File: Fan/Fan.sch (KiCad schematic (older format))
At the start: 6 parts

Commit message: Added Fan Testing Circuit
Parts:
- added Q?: ZVN3306F, Package_TO_SOT_SMD:SOT-23, symbol Transistor_FET:ZVN3306F
- added R?: R, symbol Device:R
- added V?: SQUARE_WAVE, symbol pspice:VSOURCE
- added V?: 12V, symbol pspice:VSOURCE
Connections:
- net labels added: GND
- wire segments 0 -> 14
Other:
- note added: "Vout"
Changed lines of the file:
@@
+	1    0    0    -1
+$EndComp
+$Comp
+L pspice:VSOURCE V?
+U 1 1 5E934EFD
+P 3150 4950
+F 0 "V?" H 3378 4996 50  0000 L CNN
+F 1 "SQUARE_WAVE" H 3378 4905 50  0000 L CNN
+F 2 "" H 3150 4950 50  0001 C CNN
+F 3 "~" H 3150 4950 50  0001 C CNN
+	1    3150 4950
+	1    0    0    -1
+$EndComp
+$Comp
+L power:GND #PWR?
+U 1 1 5E935667
+P 3150 5600
+F 0 "#PWR?" H 3150 5350 50  0001 C CNN
+F 1 "GND" H 3155 5427 50  0000 C CNN
+F 2 "" H 3150 5600 50  0001 C CNN
+F 3 "" H 3150 5600 50  0001 C CNN
+	1    3150 5600
+	1    0    0    -1
+$EndComp
+$Comp
+L Transistor_FET:ZVN3306F Q?
+U 1 1 5E935E89
+P 3850 4600
+F 0 "Q?" H 4054 4646 50  0000 L CNN
+F 1 "ZVN3306F" H 4054 4555 50  0000 L CNN
+F 2 "Package_TO_SOT_SMD:SOT-23" H 4050 4525 50  0001 L CIN
+F 3 "http://www.diodes.com/assets/Datasheets/ZVN3306F.pdf" H 3850 4600 50  0001 L CNN
+	1    3850 4600
+	1    0    0    -1
+$EndComp
+$Comp
+L Device:R R?
+U 1 1 5E93960D
+P 5000 4600
+F 0 "R?" H 5070 4646 50  0000 L CNN
+F 1 "R" H 5070 4555 50  0000 L CNN
+F 2 "" V 4930 4600 50  0001 C CNN
+F 3 "~" H 5000 4600 50  0001 C CNN
+	1    5000 4600
+	1    0    0    -1
+$EndComp
+$Comp
+L pspice:VSOURCE V?
+U 1 1 5E93AC04
+P 5750 5000
+F 0 "V?" H 5978 5046 50  0000 L CNN
+F 1 "12V" H 5978 4955 50  0000 L CNN
+F 2 "" H 5750 5000 50  0001 C CNN
+F 3 "~" H 5750 5000 50  0001 C CNN
+	1    5750 5000
+	1    0    0    -1
+$EndComp
+Wire Wire Line
+	5750 4700 5750 4450
+Wire Wire Line
+	5750 4450 5000 4450
+Wire Wire Line
+	3150 4650 3150 4600
+Wire Wire Line
+	3150 4600 3650 4600
+Wire Wire Line
+	3150 5250 3150 5350
+Wire Wire Line
+	3950 4800 3950 5350
+Wire Wire Line
+	3950 5350 3150 5350
+Connection ~ 3150 5350
+Wire Wire Line
+	3150 5350 3150 5600
+Wire Wire Line
+	5000 4750 5000 4800
+Wire Wire Line
+	5000 5600 5750 5600
+Text Notes 5800 5650 0    50   ~ 0
+Vout
+Wire Wire Line
+	3950 4400 4850 4400
+Wire Wire Line
+	4850 4400 4850 4800
+Wire Wire Line
+	4850 4800 5000 4800
+Connection ~ 5000 4800
+Wire Wire Line
+	5000 4800 5000 5600
+$Comp
+L power:GND #PWR?
+U 1 1 5E93E520
+P 5750 5300
+F 0 "#PWR?" H 5750 5050 50  0001 C CNN
+F 1 "GND" H 5755 5127 50  0000 C CNN
+F 2 "" H 5750 5300 50  0001 C CNN
+F 3 "" H 5750 5300 50  0001 C CNN
+	1    5750 5300
 	1    0    0    -1
 $EndComp

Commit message: more fan changes
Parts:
- removed M?: MPMOS, symbol pspice:MPMOS
- added D1: LED, symbol Device:LED
- added R2: 330, symbol Device:R
- R1: renamed from R?; value R -> 330
- gave numbers to parts that had none: 8
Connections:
- wire segments 14 -> 45
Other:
- note removed: "PMOS for simulation only"
- moved on the sheet: Q1, Q2, R1, U1, U2, V1, V2

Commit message: Added test PCB to test simulator
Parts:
- removed D1: LED, symbol Device:LED
- removed K1: HF3-06, Relay_SMD:Relay_SPDT_AXICOM_HF3Series_75ohms_Pitch1.27mm, symbol Relay:HF3-06
- added K1: RM50-xx21, Relay_THT:Relay_SPST_Finder_32.21-x300, symbol Relay:RM50-xx21
- V1: Spice_Model (none) -> pulse(0 5 0 0 0 0.05 0.1); Spice_Netlist_Enabled (none) -> Y; Spice_Primitive (none) -> V
- V2: Spice_Model (none) -> dc 12; Spice_Netlist_Enabled (none) -> Y; Spice_Primitive (none) -> V
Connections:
- net labels added: FanOut+, FanOut-, Vout
- wire segments 45 -> 46
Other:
- note removed: "Vout"
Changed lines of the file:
@@
 F 2 "" H 950 4150 50  0001 C CNN
 F 3 "~" H 950 4150 50  0001 C CNN
+F 4 "V" H 950 4150 50  0001 C CNN "Spice_Primitive"
+F 5 "pulse(0 5 0 0 0 0.05 0.1)" H 1450 4000 50  0000 C CNN "Spice_Model"
+F 6 "Y" H 950 4150 50  0001 C CNN "Spice_Netlist_Enabled"
 	1    950  4150
 	1    0    0    -1
@@
 F 2 "" H 3550 4200 50  0001 C CNN
 F 3 "~" H 3550 4200 50  0001 C CNN
+F 4 "V" H 3550 4200 50  0001 C CNN "Spice_Primitive"
+F 5 "dc 12" H 3550 4200 50  0001 C CNN "Spice_Model"
+F 6 "Y" H 3550 4200 50  0001 C CNN "Spice_Netlist_Enabled"
 	1    3550 4200
 	1    0    0    -1
@@
 Wire Wire Line
 	2800 3950 2800 4000
-Text Notes 3550 4900 0    50   ~ 0
-Vout
 Wire Wire Line
 	2650 4000 2800 4000
@@
 Wire Wire Line
 	1750 3600 2650 3600
-$Comp
-L Transistor_FET:ZVN3306F Q1
-U 1 1 5E935E89
-P 1650 3800
-F 0 "Q1" H 1854 3846 50  0000 L CNN
-F 1 "ZVN3306F" H 1854 3755 50  0000 L CNN
-F 2 "Package_TO_SOT_SMD:SOT-23" H 1850 3725 50  0001 L CIN
-F 3 "http://www.diodes.com/assets/Datasheets/ZVN3306F.pdf" H 1650 3800 50  0001 L CNN
-	1    1650 3800
-	1    0    0    -1
-$EndComp
-$Comp
-L Transistor_FET:DMP3013SFV Q2
-U 1 1 5E96184F
-P 5250 3150
-F 0 "Q2" H 5455 3196 50  0000 L CNN
-F 1 "DMP3013SFV" H 5455 3105 50  0000 L CNN
-F 2 "Package_SON:Diodes_PowerDI3333-8" H 5450 3075 50  0001 L CIN
-F 3 "https://www.diodes.com/assets/Datasheets/DMP3013SFV.pdf" V 5250 3150 50  0001 L CNN
-	1    5250 3150
-	1    0    0    -1
-$EndComp
 $Comp
 L Solar_Car_Fan:Fan_Connections U3
@@
 $EndComp
 $Comp
-L Relay:HF3-06 K1
-U 1 1 5E9341D6
-P 4750 1900
-F 0 "K1" H 5180 1946 50  0000 L CNN
-F 1 "HF3-06" H 5180 1855 50  0000 L CNN
-F 2 "Relay_SMD:Relay_SPDT_AXICOM_HF3Series_75ohms_Pitch1.27mm" H 5880 1870 50  0001 C CNN
-F 3 "http://hiqsdr.com/images/3/3e/Axicom-HF3.pdf" H 4750 1900 50  0001 C CNN
-	1    4750 1900
-	1    0    0    1
-$EndComp
-$Comp
 L Solar_Car_Fan:Power U2
 U 1 1 5E95375B
@@
 	4550 1300 4550 1600
 Wire Wire Line
-	5350 1450 4950 1450
-Wire Wire Line
-	4950 1450 4950 1500
-Wire Wire Line
-	4850 2550 4850 2200
+	5350 1450 5050 1450
 Wire Wire Line
 	5650 2700 5600 2700
@@
 Wire Wire Line
 	6350 3450 6350 1500
-Wire Wire Line
-	6350 1500 4950 1500
-Connection ~ 4950 1500
-Wire Wire Line
-	4950 1500 4950 1600
 Wire Wire Line
 	3900 2850 4150 2850
@@
 	4550 3150 5050 3150
 $Comp
-L Device:LED D1
-U 1 1 5E9B33E5
-P 6050 2800
-F 0 "D1" V 6089 2683 50  0000 R CNN
-F 1 "LED" V 5998 2683 50  0000 R CNN
-F 2 "" H 6050 2800 50  0001 C CNN
-F 3 "~" H 6050 2800 50  0001 C CNN
-	1    6050 2800
-	0    -1   -1   0
-$EndComp
-$Comp
 L Device:R R2
 U 1 1 5E9B4CDC
@@
 Wire Wire Line
 	5600 2950 5600 2700
-Wire Wire Line
-	4850 2550 5650 2550
 Connection ~ 5600 2700
 Wire Wire Line
 	5600 2700 5350 2700
+$Comp
+L Relay:RM50-xx21 K1
+U 1 1 5E989FA4
+P 4750 1900
+F 0 "K1" H 5180 1946 50  0000 L CNN
+F 1 "RM50-xx21" H 5180 1855 50  0000 L CNN
+F 2 "Relay_THT:Relay_SPST_Finder_32.21-x300" H 6020 1870 50  0001 C CNN
+F 3 "http://www.relpol.pl/en/content/download/13683/165953/file/e_RM50.pdf" H 4750 1900 50  0001 C CNN
+	1    4750 1900
+	1    0    0    -1
+$EndComp
+Wire Wire Line
+	4950 2200 4950 2550
+Wire Wire Line
+	4950 2550 5650 2550
+Wire Wire Line
+	5050 1600 5050 1500
+Wire Wire Line
+	6350 1500 5050 1500
+Connection ~ 5050 1500
+Wire Wire Line
+	5050 1500 5050 1450
+$Comp
+L Transistor_FET:ZVN3306F Q1
+U 1 1 5E9B60ED
+P 1650 3800
+F 0 "Q1" H 1854 3846 50  0000 L CNN
+F 1 "ZVN3306F" H 1854 3755 50  0000 L CNN
+F 2 "Package_TO_SOT_SMD:SOT-23" H 1850 3725 50  0001 L CIN
+F 3 "http://www.diodes.com/assets/Datasheets/ZVN3306F.pdf" H 1650 3800 50  0001 L CNN
+	1    1650 3800
+	1    0    0    -1
+$EndComp
+$Comp
+L Transistor_FET:DMP3013SFV Q2
+U 1 1 5E9BA110
+P 5250 3150
+F 0 "Q2" H 5455 3196 50  0000 L CNN
+F 1 "DMP3013SFV" H 5455 3105 50  0000 L CNN
+F 2 "Package_SON:Diodes_PowerDI3333-8" H 5450 3075 50  0001 L CIN
+F 3 "https://www.diodes.com/assets/Datasheets/DMP3013SFV.pdf" V 5250 3150 50  0001 L CNN
+	1    5250 3150
+	1    0    0    -1
+$EndComp
+Text Label 3850 4800 0    50   ~ 0
+Vout
+Text Label 5200 2550 0    50   ~ 0
+FanOut+
+Text Label 5350 2700 0    50   ~ 0
+FanOut-
+Wire Wire Line
+	6050 2650 6050 2950
 $EndSCHEMATC

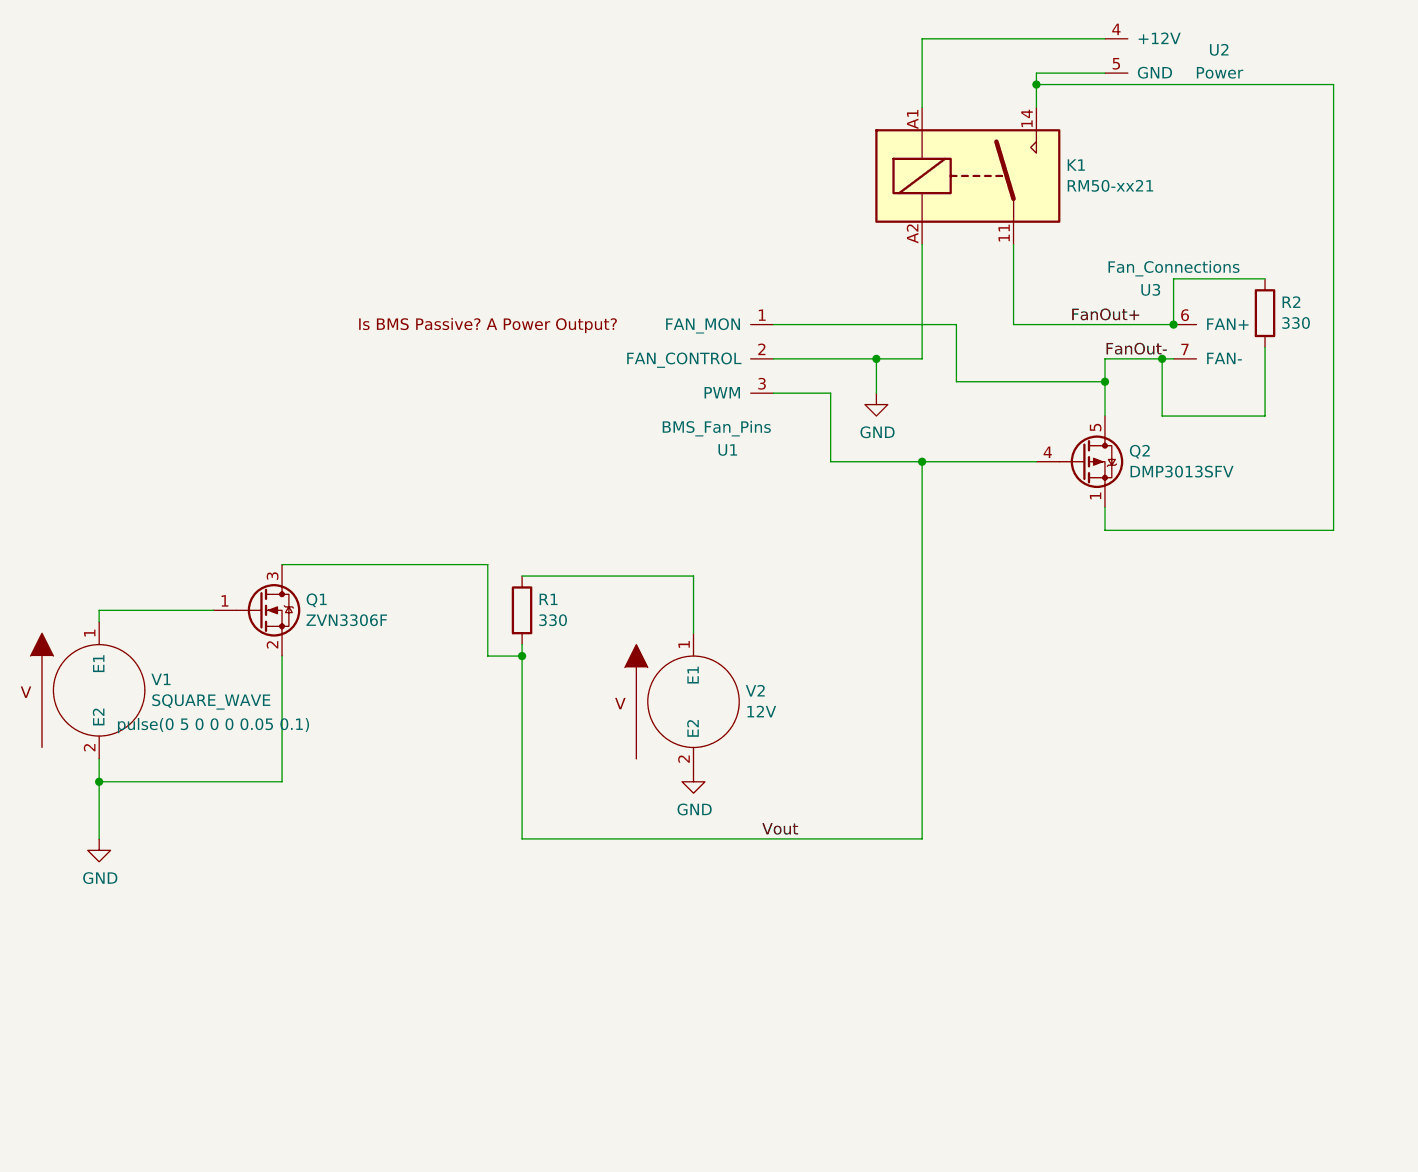
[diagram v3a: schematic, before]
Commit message: Added Multisim File for testing Fan Circuitry and MOSFET spice models
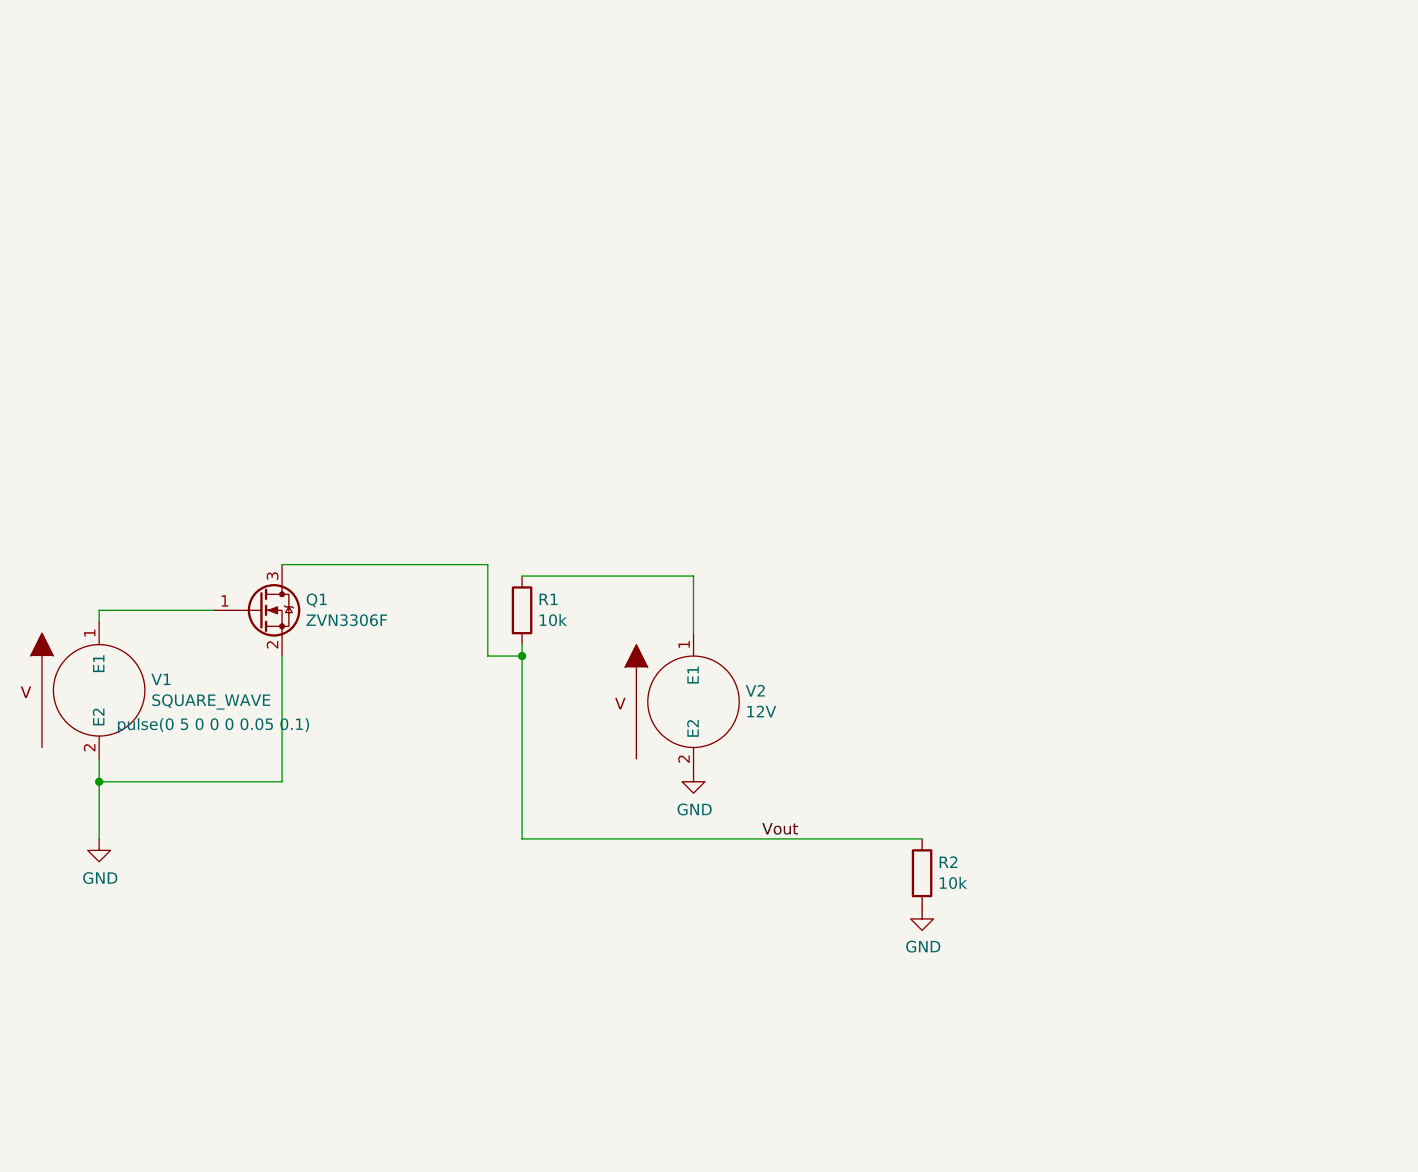
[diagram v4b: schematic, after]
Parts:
- removed K1: RM50-xx21, Relay_THT:Relay_SPST_Finder_32.21-x300, symbol Relay:RM50-xx21
- removed Q2: DMP3013SFV, Package_SON:Diodes_PowerDI3333-8, symbol Transistor_FET:DMP3013SFV
- removed U1: BMS_Fan_Pins, symbol Solar_Car_Fan:BMS_Fan_Pins
- removed U2: Power, symbol Solar_Car_Fan:Power
- removed U3: Fan_Connections, symbol Solar_Car_Fan:Fan_Connections
- Q1: Spice_Model (none) -> ZVN3306F; Spice_Netlist_Enabled (none) -> Y; Spice_Primitive (none) -> M
- R1, R2: value 330 -> 10k
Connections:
- net FanOut+ is gone; now on net Vout: R2.1
- net FanOut- is gone; now on net GND: R2.2
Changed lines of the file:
@@
 P 2800 3800
 F 0 "R1" H 2870 3846 50  0000 L CNN
-F 1 "330" H 2870 3755 50  0000 L CNN
+F 1 "10k" H 2870 3755 50  0000 L CNN
 F 2 "" V 2730 3800 50  0001 C CNN
 F 3 "~" H 2800 3800 50  0001 C CNN
@@
 Wire Wire Line
 	2800 4000 2800 4800
+Wire Wire Line
+	2650 3600 2650 4000
+Wire Wire Line
+	1750 3600 2650 3600
+Wire Wire Line
+	2800 4800 4550 4800
+$Comp
+L Transistor_FET:ZVN3306F Q1
+U 1 1 5E9B60ED
+P 1650 3800
+F 0 "Q1" H 1854 3846 50  0000 L CNN
+F 1 "ZVN3306F" H 1854 3755 50  0000 L CNN
+F 2 "Package_TO_SOT_SMD:SOT-23" H 1850 3725 50  0001 L CIN
+F 3 "http://www.diodes.com/assets/Datasheets/ZVN3306F.pdf" H 1650 3800 50  0001 L CNN
+F 4 "M" H 1650 3800 50  0001 C CNN "Spice_Primitive"
+F 5 "ZVN3306F" H 1650 3800 50  0001 C CNN "Spice_Model"
+F 6 "Y" H 1650 3800 50  0001 C CNN "Spice_Netlist_Enabled"
+	1    1650 3800
+	1    0    0    -1
+$EndComp
+Text Label 3850 4800 0    50   ~ 0
+Vout
 $Comp
 L power:GND #PWR02
@@
 	1    0    0    -1
 $EndComp
-Wire Wire Line
-	2650 3600 2650 4000
-Wire Wire Line
-	1750 3600 2650 3600
-$Comp
-L Solar_Car_Fan:Fan_Connections U3
-U 1 1 5E952CAF
-P 6050 2800
-F 0 "U3" H 6550 2400 50  0000 C CNN
-F 1 "Fan_Connections" H 6450 2300 50  0000 C CNN
-F 2 "" H 6100 2950 50  0001 C CNN
-F 3 "" H 6100 2950 50  0001 C CNN
-	1    6050 2800
-	-1   0    0    1
-$EndComp
-$Comp
-L Solar_Car_Fan:BMS_Fan_Pins U1
-U 1 1 5E952447
-P 3650 3150
-F 0 "U1" H 3700 3100 50  0000 C CNN
-F 1 "BMS_Fan_Pins" H 3650 3000 50  0000 C CNN
-F 2 "" H 3650 3150 50  0001 C CNN
-F 3 "" H 3650 3150 50  0001 C CNN
-	1    3650 3150
-	1    0    0    1
-$EndComp
-$Comp
-L Solar_Car_Fan:Power U2
-U 1 1 5E95375B
-P 5450 1050
-F 0 "U2" H 5050 750 50  0000 C CNN
-F 1 "Power" H 5050 650 50  0000 C CNN
-F 2 "" H 5450 1050 50  0001 C CNN
-F 3 "" H 5450 1050 50  0001 C CNN
-	1    5450 1050
-	-1   0    0    -1
-$EndComp
-Wire Wire Line
-	5350 1300 4550 1300
-Wire Wire Line
-	4550 1300 4550 1600
-Wire Wire Line
-	5350 1450 5050 1450
-Wire Wire Line
-	5650 2700 5600 2700
-Wire Wire Line
-	5350 2700 5350 2800
-Wire Wire Line
-	5350 3350 5350 3450
-Wire Wire Line
-	5350 3450 6350 3450
-Wire Wire Line
-	6350 3450 6350 1500
-Wire Wire Line
-	3900 2850 4150 2850
-Wire Wire Line
-	4150 2850 4150 3150
-Wire Wire Line
-	4150 3150 4550 3150
-Wire Wire Line
-	3900 2700 4350 2700
-Wire Wire Line
-	4550 2700 4550 2200
-Wire Wire Line
-	3900 2550 4700 2550
-Wire Wire Line
-	4700 2550 4700 2800
-Wire Wire Line
-	4700 2800 5350 2800
-Connection ~ 5350 2800
-Wire Wire Line
-	5350 2800 5350 2950
-$Comp
-L power:GND #PWR03
-U 1 1 5E9B01F0
-P 4350 2850
-F 0 "#PWR03" H 4350 2600 50  0001 C CNN
-F 1 "GND" H 4355 2677 50  0000 C CNN
-F 2 "" H 4350 2850 50  0001 C CNN
-F 3 "" H 4350 2850 50  0001 C CNN
-	1    4350 2850
-	1    0    0    -1
-$EndComp
-Wire Wire Line
-	4350 2850 4350 2700
-Connection ~ 4350 2700
-Wire Wire Line
-	4350 2700 4550 2700
-Wire Wire Line
-	4550 4800 4550 3150
-Wire Wire Line
-	2800 4800 4550 4800
-Connection ~ 4550 3150
-Wire Wire Line
-	4550 3150 5050 3150
 $Comp
 L Device:R R2
-U 1 1 5E9B4CDC
-P 6050 2500
-F 0 "R2" H 6120 2546 50  0000 L CNN
-F 1 "330" H 6120 2455 50  0000 L CNN
-F 2 "" V 5980 2500 50  0001 C CNN
-F 3 "~" H 6050 2500 50  0001 C CNN
-	1    6050 2500
-	1    0    0    -1
-$EndComp
-Wire Wire Line
-	5650 2550 5650 2350
-Wire Wire Line
-	5650 2350 6050 2350
-Connection ~ 5650 2550
-Wire Wire Line
-	6050 2950 5600 2950
-Wire Wire Line
-	5600 2950 5600 2700
-Connection ~ 5600 2700
-Wire Wire Line
-	5600 2700 5350 2700
-$Comp
-L Relay:RM50-xx21 K1
-U 1 1 5E989FA4
-P 4750 1900
-F 0 "K1" H 5180 1946 50  0000 L CNN
-F 1 "RM50-xx21" H 5180 1855 50  0000 L CNN
-F 2 "Relay_THT:Relay_SPST_Finder_32.21-x300" H 6020 1870 50  0001 C CNN
-F 3 "http://www.relpol.pl/en/content/download/13683/165953/file/e_RM50.pdf" H 4750 1900 50  0001 C CNN
-	1    4750 1900
-	1    0    0    -1
-$EndComp
-Wire Wire Line
-	4950 2200 4950 2550
-Wire Wire Line
-	4950 2550 5650 2550
-Wire Wire Line
-	5050 1600 5050 1500
-Wire Wire Line
-	6350 1500 5050 1500
-Connection ~ 5050 1500
-Wire Wire Line
-	5050 1500 5050 1450
-$Comp
-L Transistor_FET:ZVN3306F Q1
-U 1 1 5E9B60ED
-P 1650 3800
-F 0 "Q1" H 1854 3846 50  0000 L CNN
-F 1 "ZVN3306F" H 1854 3755 50  0000 L CNN
-F 2 "Package_TO_SOT_SMD:SOT-23" H 1850 3725 50  0001 L CIN
-F 3 "http://www.diodes.com/assets/Datasheets/ZVN3306F.pdf" H 1650 3800 50  0001 L CNN
-	1    1650 3800
+U 1 1 5E9D1C4A
+P 4550 4950
+F 0 "R2" H 4620 4996 50  0000 L CNN
+F 1 "10k" H 4620 4905 50  0000 L CNN
+F 2 "" V 4480 4950 50  0001 C CNN
+F 3 "~" H 4550 4950 50  0001 C CNN
+	1    4550 4950
 	1    0    0    -1
 $EndComp
 $Comp
-L Transistor_FET:DMP3013SFV Q2
-U 1 1 5E9BA110
-P 5250 3150
-F 0 "Q2" H 5455 3196 50  0000 L CNN
-F 1 "DMP3013SFV" H 5455 3105 50  0000 L CNN
-F 2 "Package_SON:Diodes_PowerDI3333-8" H 5450 3075 50  0001 L CIN
-F 3 "https://www.diodes.com/assets/Datasheets/DMP3013SFV.pdf" V 5250 3150 50  0001 L CNN
-	1    5250 3150
+L power:GND #PWR03
+U 1 1 5E9D21C2
+P 4550 5100
+F 0 "#PWR03" H 4550 4850 50  0001 C CNN
+F 1 "GND" H 4555 4927 50  0000 C CNN
+F 2 "" H 4550 5100 50  0001 C CNN
+F 3 "" H 4550 5100 50  0001 C CNN
+	1    4550 5100
 	1    0    0    -1
 $EndComp
-Text Label 3850 4800 0    50   ~ 0
-Vout
-Text Label 5200 2550 0    50   ~ 0
-FanOut+
-Text Label 5350 2700 0    50   ~ 0
-FanOut-
-Wire Wire Line
-	6050 2650 6050 2950
 $EndSCHEMATC
